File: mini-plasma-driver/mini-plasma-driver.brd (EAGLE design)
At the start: 100 x 80 mm, 93 parts, among them IC1 IR21844D, IC2 74LS19N, IC3 NE555N, IC5 IR21844D, J1 12v IN, Q1 IRF640, Q2 IRF640, Q3 2N2369, Q4 2N2369, Q5 IRF640, Q6 IRF640

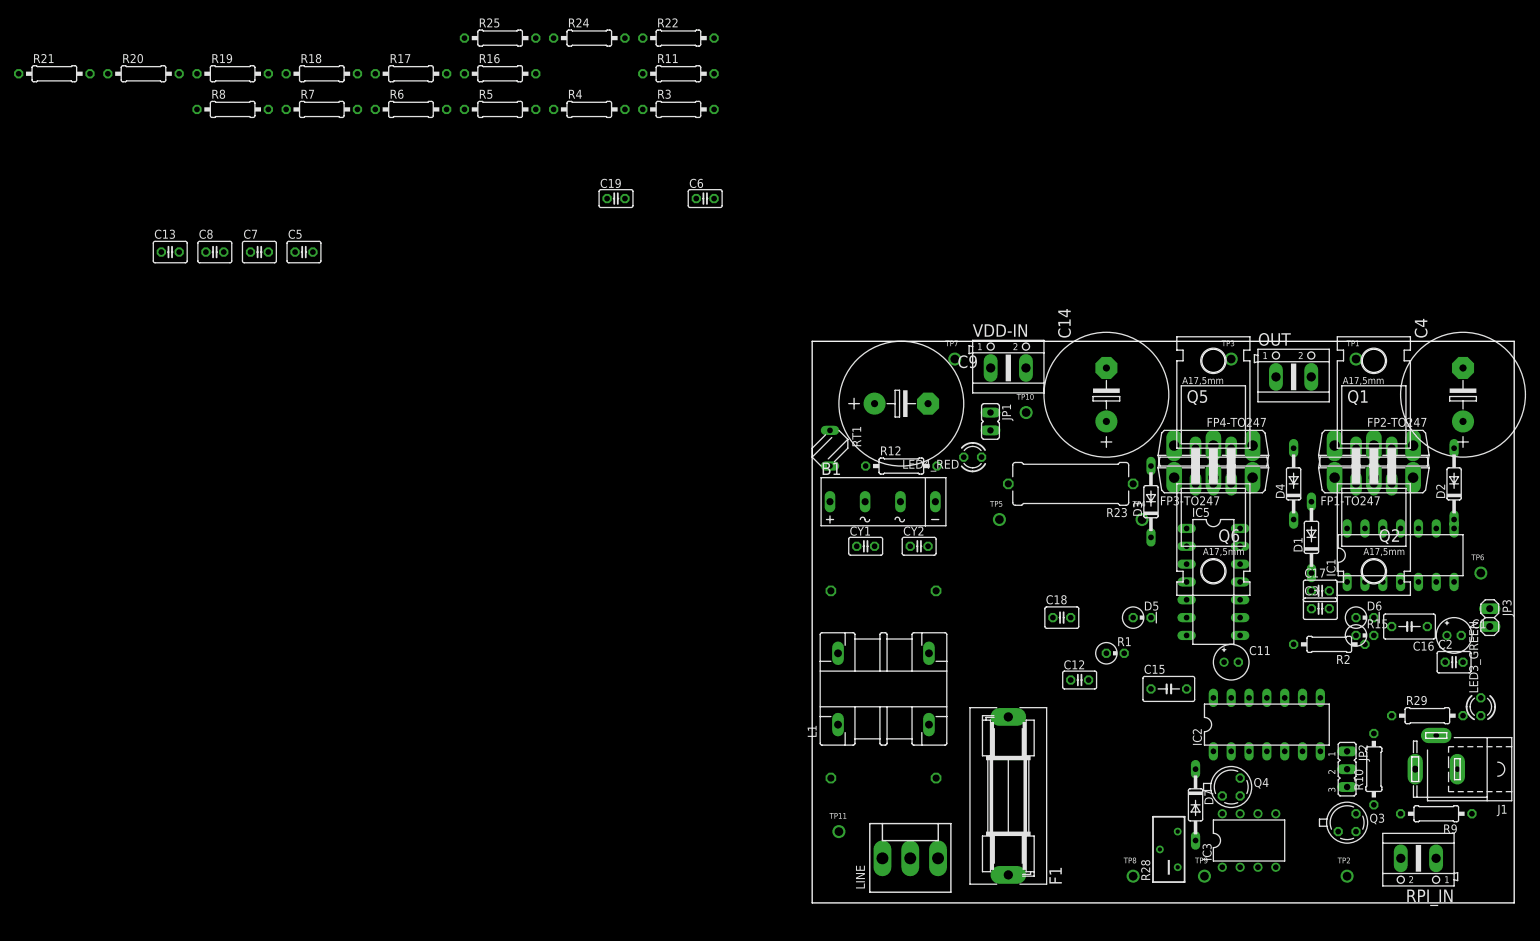
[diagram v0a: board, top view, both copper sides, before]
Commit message: First pass at placement, with schematic tweaks. Size of board not specified; Choke L1 drawing pinouts are incorrect + need to verif footprint
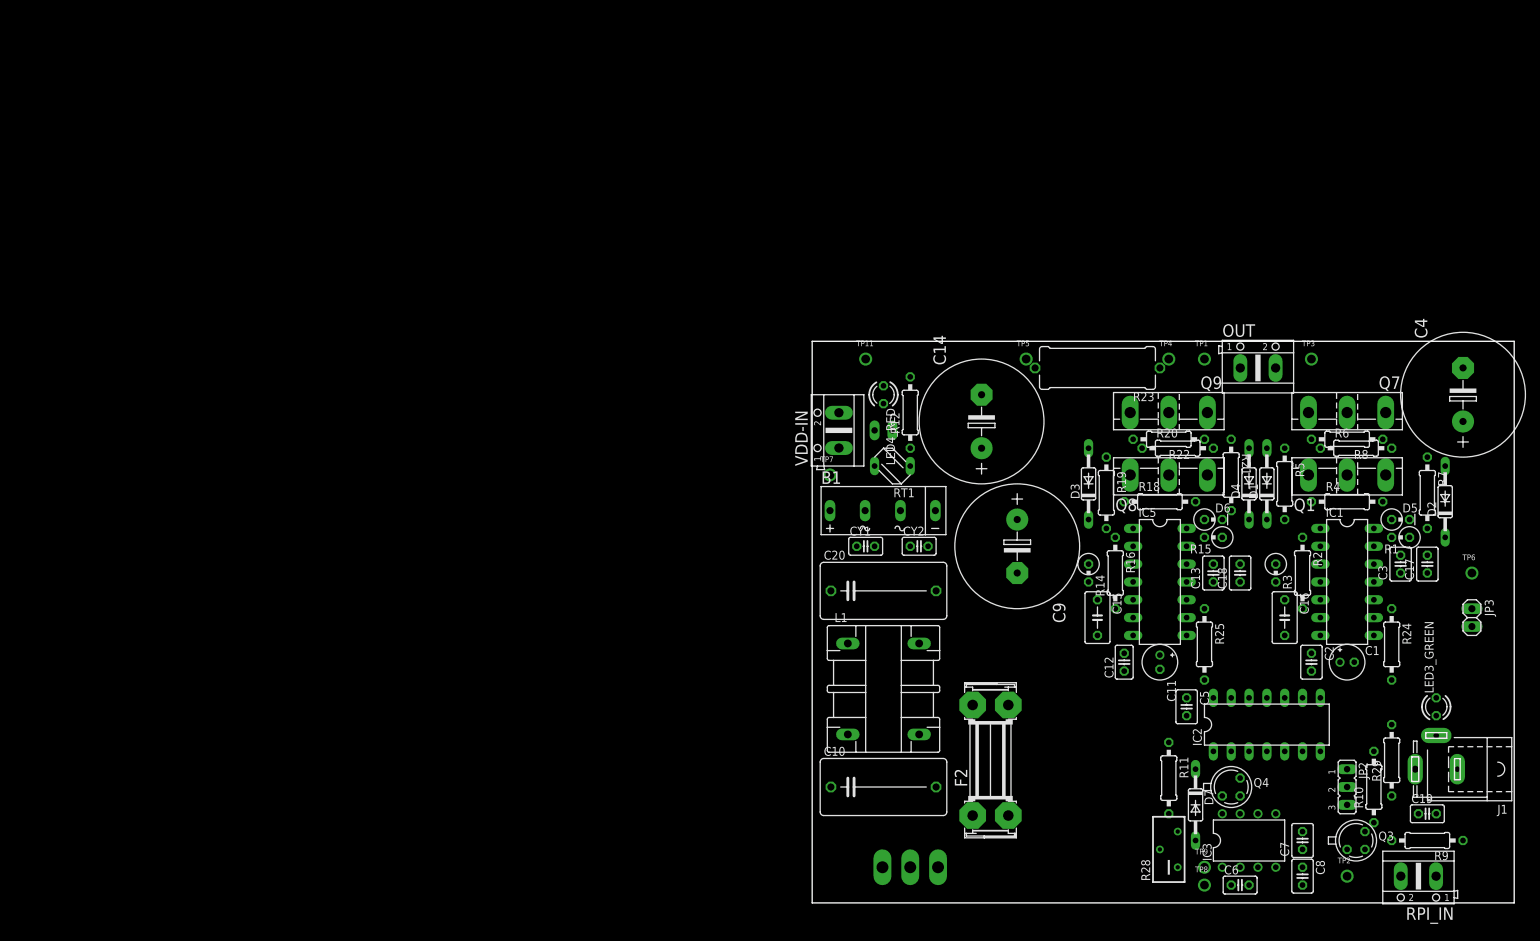
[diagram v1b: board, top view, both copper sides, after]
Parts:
- removed F1: 4A, fuse:SH22,5A
- removed FP1-TO247, FP2-TO247, FP3-TO247, FP4-TO247: IRFPC40, transistor-power:TO247BV
- removed Q2, Q5, Q6: IRF640, transistor-fet:TO220
- removed R17: ?, rcl:0207/10
- removed TP10: (no value), microbuilder:1X01_ROUND
- added F2: 4A, fuse:SHK20Q
- added Q7, Q8, Q9: STH60N10W, transistor-power:TO-247AD-V
- added R14: 0, rcl:0309V
- Q1: value IRF640 -> STH60N10W; device transistor-fet:TO220 -> transistor-power:TO-247AD-V
- R24, R25: value 10 1W -> 0
- R3: value ? -> 0; device rcl:0207/10 -> rcl:0309V
- moved C8 178.6 mm to (69.8, 3.81), turned to 270 degrees
- moved R21 177.1 mm to (59.7, 61.0), turned to 270.1 degrees
- moved C7 170.6 mm to (69.8, 8.89), turned to 90 degrees
- moved R7 166.7 mm to (87.6, 58.4), turned to 270 degrees
- moved R8 165.6 mm to (76.2, 66.0), turned to 180 degrees
- moved R20 156.7 mm to (52.1, 64.8)
- moved C13 155.5 mm to (57.1, 47.0), turned to 90 degrees
- moved C19 145.0 mm to (87.6, 12.7)
- moved R24 143.3 mm to (82.5, 36.8), turned to 270 degrees
- moved R6 143.0 mm to (77.5, 64.8)
- moved C5 141.4 mm to (53.3, 27.9), turned to 270 degrees
- moved R19 138.0 mm to (41.9, 58.4), turned to 270 degrees
- moved R18 134.0 mm to (49.5, 57.1)
- moved R25 132.4 mm to (55.9, 36.8), turned to 270 degrees
- moved C6 124.0 mm to (61.0, 2.54)
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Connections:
- removed net N$33: JP1.1, TP7.1, VDD-IN.1
- new net N$2: C9.+, JP1.2, RT1.1
- net 12V: now also C12.2; no longer C12.1
- net GND: now also C12.1, R14.1, R3.1; no longer C12.2, R17.2, R3.2
- net N$18: now also F2.2A, F2.2B; no longer F1.2
- net N$19: now also F2.1A, F2.1B; no longer F1.1
- net N$20: now also L1.4; no longer L1.2
- net N$22: now also L1.2; no longer L1.4
- net N$26: now also R14.2; no longer R17.1
- net N$28: now also Q8.G; no longer FP3-TO247.G, Q5.1
- net N$30: now also Q9.G; no longer FP4-TO247.G, Q6.1
- net N$35: now also Q7.S, Q9.S; no longer FP2-TO247.S, FP4-TO247.S, Q2.3, Q6.3
- net N$6: now also R3.2; no longer R3.1
- net N$7: now also Q1.G; no longer Q1.1
- net N$9: now also Q7.G; no longer Q2.1
- net O1: now also Q1.S, Q7.D; no longer FP1-TO247.S, FP2-TO247.D, Q1.3, Q2.2
- net O2: now also Q8.S, Q9.D; no longer FP3-TO247.S, FP4-TO247.D, Q5.3, Q6.2
- net VDD: now also JP1.1, Q1.D, Q8.D, TP7.1, VDD-IN.1; no longer C9.+, FP1-TO247.D, FP3-TO247.D, JP1.2, Q1.2, Q5.2, RT1.1
- net VDD-: no longer TP10.1

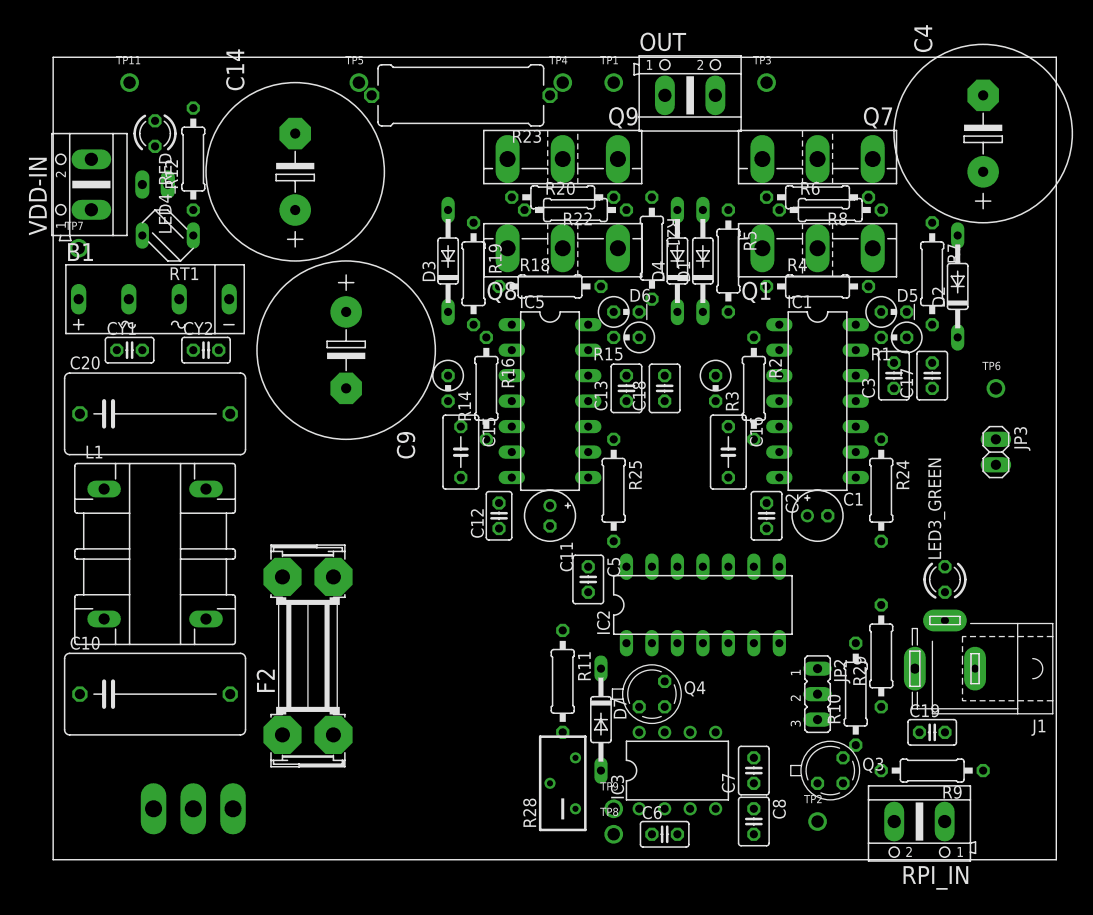
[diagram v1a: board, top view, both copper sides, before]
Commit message: add mounting holes
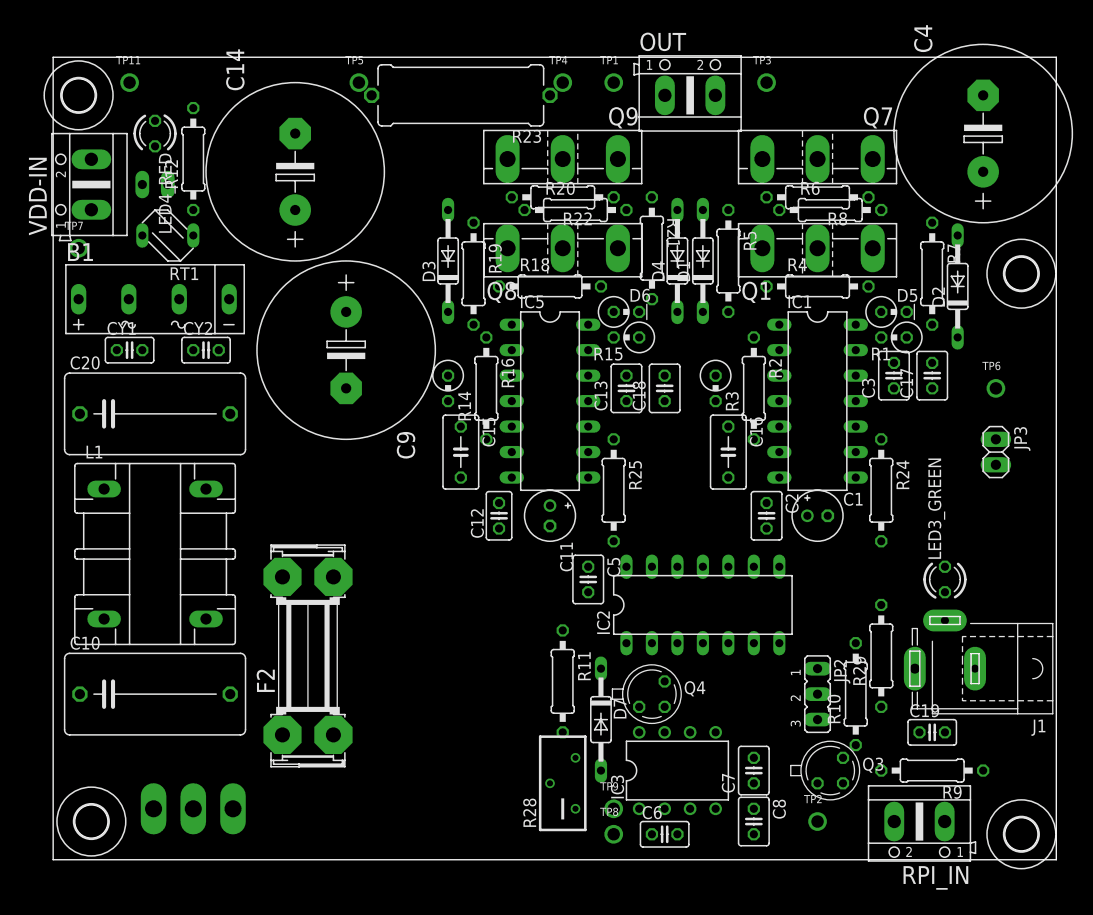
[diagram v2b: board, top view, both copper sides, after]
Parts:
- added H1, H2, H3, H4: MOUNT-HOLE3.3, holes:3,3
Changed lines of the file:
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@@
 <layers>
 <layer number="1" name="Top" color="4" fill="1" visible="yes" active="yes"/>
+<layer number="2" name="Route2" color="1" fill="3" visible="no" active="no"/>
+<layer number="3" name="Route3" color="4" fill="3" visible="no" active="no"/>
+<layer number="4" name="Route4" color="1" fill="4" visible="no" active="no"/>
+<layer number="5" name="Route5" color="4" fill="4" visible="no" active="no"/>
+<layer number="6" name="Route6" color="1" fill="8" visible="no" active="no"/>
+<layer number="7" name="Route7" color="4" fill="8" visible="no" active="no"/>
+<layer number="8" name="Route8" color="1" fill="2" visible="no" active="no"/>
+<layer number="9" name="Route9" color="4" fill="2" visible="no" active="no"/>
+<layer number="10" name="Route10" color="1" fill="7" visible="no" active="no"/>
+<layer number="11" name="Route11" color="4" fill="7" visible="no" active="no"/>
+<layer number="12" name="Route12" color="1" fill="5" visible="no" active="no"/>
+<layer number="13" name="Route13" color="4" fill="5" visible="no" active="no"/>
+<layer number="14" name="Route14" color="1" fill="6" visible="no" active="no"/>
+<layer number="15" name="Route15" color="4" fill="6" visible="no" active="no"/>
 <layer number="16" name="Bottom" color="1" fill="1" visible="yes" active="yes"/>
 <layer number="17" name="Pads" color="2" fill="1" visible="yes" active="yes"/>
@@
 </class>
 </classes>
-<designrules name="default">
+<designrules name="oshpark-2layer-2017-05">
 <description language="de">&lt;b&gt;EAGLE Design Rules&lt;/b&gt;
 &lt;p&gt;
@@
 Einstellungen hier und speichern die Design Rules unter
 einem neuen Namen ab.</description>
-<description language="en">&lt;b&gt;EAGLE Design Rules&lt;/b&gt;
+<description language="en">&lt;b&gt;Laen's PCB Order Design Rules&lt;/b&gt;
 &lt;p&gt;
-The default Design Rules have been set to cover
-a wide range of applications. Your particular design
-may have different requirements, so please make the
-necessary adjustments and save your customized
-design rules under a new name.</description>
+Please make sure your boards conform to these design rules.</description>
 <param name="layerSetup" value="(1*16)"/>
-<param name="mtCopper" value="0.035mm 0.035mm 0.035mm 0.035mm 0.035mm 0.035mm 0.035mm 0.035mm 0.035mm 0.035mm 0.035mm 0.035mm 0.035mm 0.035mm 0.035mm 0.035mm"/>
-<param name="mtIsolate" value="1.5mm 0.15mm 0.2mm 0.15mm 0.2mm 0.15mm 0.2mm 0.15mm 0.2mm 0.15mm 0.2mm 0.15mm 0.2mm 0.15mm 0.2mm"/>
+<param name="mtCopper" value="0.0356mm 0.0356mm 0.0356mm 0.0356mm 0.0356mm 0.0356mm 0.0356mm 0.0356mm 0.0356mm 0.0356mm 0.0356mm 0.0356mm 0.0356mm 0.0356mm 0.0356mm 0.0356mm"/>
+<param name="mtIsolate" value="1.5011mm 0.1499mm 0.2007mm 0.1499mm 0.2007mm 0.1499mm 0.2007mm 0.1499mm 0.2007mm 0.1499mm 0.2007mm 0.1499mm 0.2007mm 0.1499mm 0.2007mm"/>
 <param name="mdWireWire" value="6mil"/>
 <param name="mdWirePad" value="6mil"/>
@@
 <param name="mdSmdVia" value="6mil"/>
 <param name="mdSmdSmd" value="6mil"/>
-<param name="mdViaViaSameLayer" value="6mil"/>
+<param name="mdViaViaSameLayer" value="8mil"/>
 <param name="mnLayersViaInSmd" value="2"/>
-<param name="mdCopperDimension" value="40mil"/>
+<param name="mdCopperDimension" value="15mil"/>
 <param name="mdDrill" value="6mil"/>
 <param name="mdSmdStop" value="0mil"/>
 <param name="msWidth" value="6mil"/>
-<param name="msDrill" value="0.35mm"/>
-<param name="msMicroVia" value="9.99mm"/>
+<param name="msDrill" value="13mil"/>
+<param name="msMicroVia" value="13mil"/>
 <param name="msBlindViaRatio" value="0.5"/>
 <param name="rvPadTop" value="0.25"/>
@@
 <param name="rvMicroViaOuter" value="0.25"/>
 <param name="rvMicroViaInner" value="0.25"/>
-<param name="rlMinPadTop" value="10mil"/>
+<param name="rlMinPadTop" value="7mil"/>
 <param name="rlMaxPadTop" value="20mil"/>
-<param name="rlMinPadInner" value="10mil"/>
+<param name="rlMinPadInner" value="7mil"/>
 <param name="rlMaxPadInner" value="20mil"/>
-<param name="rlMinPadBottom" value="10mil"/>
+<param name="rlMinPadBottom" value="7mil"/>
 <param name="rlMaxPadBottom" value="20mil"/>
-<param name="rlMinViaOuter" value="8mil"/>
+<param name="rlMinViaOuter" value="7mil"/>
 <param name="rlMaxViaOuter" value="20mil"/>
-<param name="rlMinViaInner" value="8mil"/>
+<param name="rlMinViaInner" value="7mil"/>
 <param name="rlMaxViaInner" value="20mil"/>
 <param name="rlMinMicroViaOuter" value="4mil"/>
@@
 <param name="mvStopFrame" value="1"/>
 <param name="mvCreamFrame" value="0"/>
-<param name="mlMinStopFrame" value="4mil"/>
-<param name="mlMaxStopFrame" value="4mil"/>
+<param name="mlMinStopFrame" value="2.5mil"/>
+<param name="mlMaxStopFrame" value="2.5mil"/>
 <param name="mlMinCreamFrame" value="0mil"/>
 <param name="mlMaxCreamFrame" value="0mil"/>
@@
 <attribute name="SPICEPREFIX" value="R" x="39.37" y="46.99" size="1.778" layer="27" rot="R270" display="off"/>
 </element>
+<element name="H1" library="holes" library_urn="urn:adsk.eagle:library:237" package="3,3" package3d_urn="urn:adsk.eagle:package:14278/1" value="MOUNT-HOLE3.3" x="3.81" y="3.81"/>
+<element name="H2" library="holes" library_urn="urn:adsk.eagle:library:237" package="3,3" package3d_urn="urn:adsk.eagle:package:14278/1" value="MOUNT-HOLE3.3" x="2.54" y="76.2"/>
+<element name="H3" library="holes" library_urn="urn:adsk.eagle:library:237" package="3,3" package3d_urn="urn:adsk.eagle:package:14278/1" value="MOUNT-HOLE3.3" x="96.52" y="2.54"/>
+<element name="H4" library="holes" library_urn="urn:adsk.eagle:library:237" package="3,3" package3d_urn="urn:adsk.eagle:package:14278/1" value="MOUNT-HOLE3.3" x="96.52" y="58.42"/>
 </elements>
 <signals>
